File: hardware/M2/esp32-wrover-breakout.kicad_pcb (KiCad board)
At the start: 2 copper layers, 44 x 22 mm, 10 parts, among them IC1 ESP32-WROVER-E_M213EH6464PH3Q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, J1 Edge_Conn_NGFF_E_Key, Q1 MUN5214DW1T1G, U1 XC6220B331MR

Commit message: A couple finishing touches
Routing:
- net GND: track 33.0 -> 32.5 mm
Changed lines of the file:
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@@
     (thickness 1.6)
     (drawings 10)
-    (tracks 320)
+    (tracks 318)
     (zones 0)
     (modules 10)
@@
   (layers
     (0 F.Cu signal)
-    (31 B.Cu signal)
+    (31 B.Cu signal hide)
     (32 B.Adhes user hide)
     (33 F.Adhes user hide)
@@
   (segment (start 68.528 29.399) (end 68.528 28.939) (width 0.25) (layer F.Cu) (net 1))
   (segment (start 68.528 28.939) (end 69.255979 28.211021) (width 0.25) (layer F.Cu) (net 1))
-  (via (at 68.568 31.099) (size 0.508) (drill 0.254) (layers F.Cu B.Cu) (net 1))
-  (segment (start 68.528 29.399) (end 68.528 31.059) (width 0.25) (layer F.Cu) (net 1))
-  (segment (start 68.528 31.059) (end 68.568 31.099) (width 0.25) (layer F.Cu) (net 1))
   (via (at 63.983 35.064) (size 0.508) (drill 0.254) (layers F.Cu B.Cu) (net 1))
   (segment (start 62.863 35.064) (end 63.983 35.064) (width 0.25) (layer F.Cu) (net 1))
@@
   (segment (start 61.028 35.064) (end 61.028 33.959) (width 0.25) (layer F.Cu) (net 1))
   (segment (start 61.028 33.959) (end 61.018 33.949) (width 0.25) (layer F.Cu) (net 1))
-  (via (at 61.018 40.049) (size 0.508) (drill 0.254) (layers F.Cu B.Cu) (net 1))
-  (segment (start 61.028 38.734) (end 61.028 40.039) (width 0.25) (layer F.Cu) (net 1))
-  (segment (start 61.028 40.039) (end 61.018 40.049) (width 0.25) (layer F.Cu) (net 1))
   (via (at 58.068 35.049) (size 0.508) (drill 0.254) (layers F.Cu B.Cu) (net 1))
   (segment (start 59.193 35.064) (end 58.083 35.064) (width 0.25) (layer F.Cu) (net 1))
@@
   (segment (start 68.528 45.009) (end 68.518 44.999) (width 0.25) (layer F.Cu) (net 1))
   (via (at 35.968 47.199) (size 0.508) (drill 0.254) (layers F.Cu B.Cu) (net 1))
+  (via (at 61.028 39.838998) (size 0.508) (drill 0.254) (layers F.Cu B.Cu) (net 1))
+  (segment (start 61.028 38.734) (end 61.028 39.838998) (width 0.25) (layer F.Cu) (net 1))
+  (via (at 68.528 30.809) (size 0.508) (drill 0.254) (layers F.Cu B.Cu) (net 1))
+  (segment (start 68.528 29.399) (end 68.528 30.809) (width 0.25) (layer F.Cu) (net 1))
   (via (at 53.468 32.099) (size 0.508) (drill 0.254) (layers F.Cu B.Cu) (net 3))
   (via (at 54.868 32.099) (size 0.508) (drill 0.254) (layers F.Cu B.Cu) (net 3))

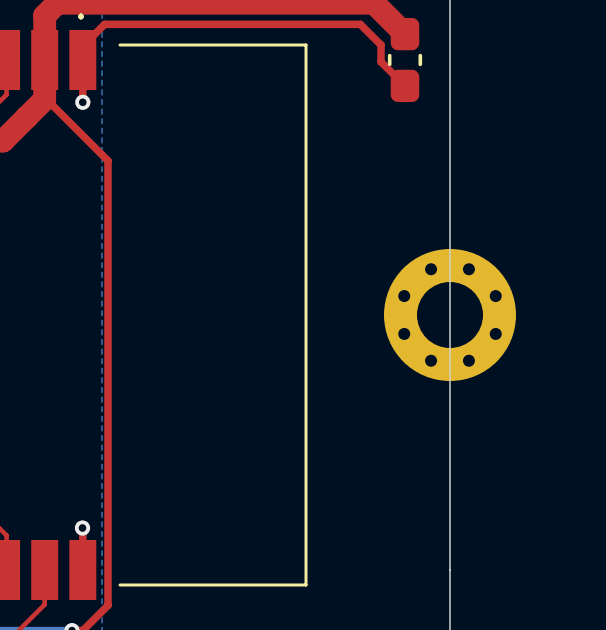
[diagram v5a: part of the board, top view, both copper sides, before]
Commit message: Fix mounting hole size
Allow for the 3mm bushing.
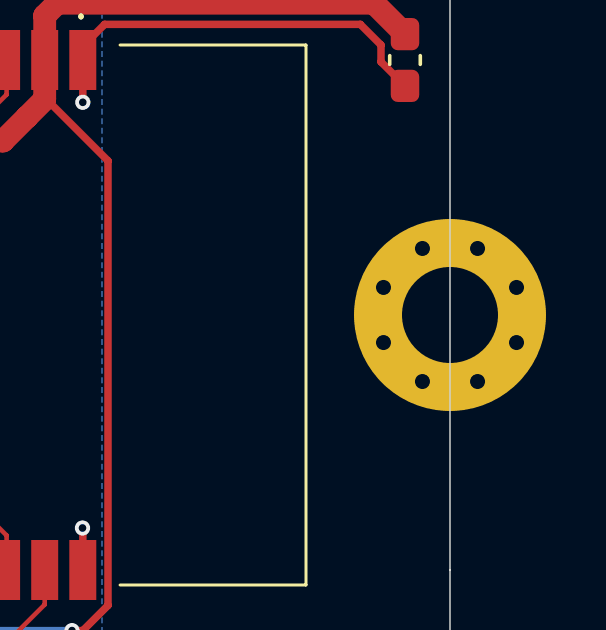
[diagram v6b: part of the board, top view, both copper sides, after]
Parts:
- REF**: value MountingHole_2.2mm_M2_Pad_Via -> MountingHole_3.2mm_M3_Pad_Via; footprint MountingHole:MountingHole_2.2mm_M2_Pad_Via -> MountingHole:MountingHole_3.2mm_M3_Pad_Via
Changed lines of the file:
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@@
     (add_net "Net-(U1-Pad4)")
+  )
+  (module MountingHole:MountingHole_3.2mm_M3_Pad_Via (layer F.Cu)
+    (at 80.768 37.899 22.5)
+    (descr "Mounting Hole 3.2mm, M3")
+    (tags "mounting hole 3.2mm m3")
+    (attr virtual)
+    (fp_text reference REF** (at 0 -3.2 22.5) (layer F.SilkS) hide
+      (effects (font (size 1 1) (thickness 0.15)))
+    )
+    (fp_text value MountingHole_3.2mm_M3_Pad_Via (at 0 3.2 22.5) (layer F.Fab)
+      (effects (font (size 1 1) (thickness 0.15)))
+    )
+    (fp_circle (center 0 0) (end 3.45 0) (layer F.CrtYd) (width 0.05))
+    (fp_circle (center 0 0) (end 3.2 0) (layer Cmts.User) (width 0.15))
+    (fp_text user %R (at 0.3 0 22.5) (layer F.Fab)
+      (effects (font (size 1 1) (thickness 0.15)))
+    )
+    (pad 1 thru_hole circle (at 1.697056 -1.697056 22.5) (size 0.8 0.8) (drill 0.5) (layers *.Cu *.Mask))
+    (pad 1 thru_hole circle (at 0 -2.4 22.5) (size 0.8 0.8) (drill 0.5) (layers *.Cu *.Mask))
+    (pad 1 thru_hole circle (at -1.697056 -1.697056 22.5) (size 0.8 0.8) (drill 0.5) (layers *.Cu *.Mask))
+    (pad 1 thru_hole circle (at -2.4 0 22.5) (size 0.8 0.8) (drill 0.5) (layers *.Cu *.Mask))
+    (pad 1 thru_hole circle (at -1.697056 1.697056 22.5) (size 0.8 0.8) (drill 0.5) (layers *.Cu *.Mask))
+    (pad 1 thru_hole circle (at 0 2.4 22.5) (size 0.8 0.8) (drill 0.5) (layers *.Cu *.Mask))
+    (pad 1 thru_hole circle (at 1.697056 1.697056 22.5) (size 0.8 0.8) (drill 0.5) (layers *.Cu *.Mask))
+    (pad 1 thru_hole circle (at 2.4 0 22.5) (size 0.8 0.8) (drill 0.5) (layers *.Cu *.Mask))
+    (pad 1 thru_hole circle (at 0 0 22.5) (size 6.4 6.4) (drill 3.2) (layers *.Cu *.Mask))
   )
   (module ESP32-WROVER-E:ESP32WROVEREM213EH6464PH3Q0 (layer F.Cu)
@@
       (effects (font (size 1 1) (thickness 0.15)))
     )
-    (fp_arc (start 10.425 -3.5) (end 9.925 -3.5) (angle 90) (layer Edge.Cuts) (width 0.05))
-    (fp_arc (start 2.625 -2.9) (end 2.025 -2.9) (angle 180) (layer Edge.Cuts) (width 0.05))
-    (fp_arc (start -10.425 -3.5) (end -10.425 -4) (angle 90) (layer Edge.Cuts) (width 0.05))
     (fp_line (start -11 -4) (end -10.425 -4) (layer Edge.Cuts) (width 0.05))
     (fp_line (start -9.925 -3.5) (end -9.925 0) (layer Edge.Cuts) (width 0.05))
@@
     (fp_poly (pts (xy 3.225 0) (xy 9.925 0) (xy 9.925 -2) (xy 3.225 -2)) (layer F.Mask) (width 0.1))
     (fp_poly (pts (xy 3.225 0) (xy 9.925 0) (xy 9.925 -2.5) (xy 3.225 -2.5)) (layer B.Mask) (width 0.1))
+    (fp_arc (start 10.425 -3.5) (end 9.925 -3.5) (angle 90) (layer Edge.Cuts) (width 0.05))
+    (fp_arc (start 2.625 -2.9) (end 2.025 -2.9) (angle 180) (layer Edge.Cuts) (width 0.05))
+    (fp_arc (start -10.425 -3.5) (end -10.425 -4) (angle 90) (layer Edge.Cuts) (width 0.05))
     (pad 75 smd rect (at -9.25 -1.275 270) (size 0.35 1.45) (layers F.Cu)
       (net 1 GND))
@@
     (pad 1 smd rect (at 9.25 -1.275 270) (size 0.35 1.45) (layers F.Cu)
       (net 1 GND))
-  )
-  (module MountingHole:MountingHole_2.2mm_M2_Pad_Via (layer F.Cu)
-    (at 80.768 37.899 22.5)
-    (descr "Mounting Hole 2.2mm, M2")
-    (tags "mounting hole 2.2mm m2")
-    (attr virtual)
-    (fp_text reference REF** (at 0 -3.2 22.5) (layer F.SilkS) hide
-      (effects (font (size 1 1) (thickness 0.15)))
-    )
-    (fp_text value MountingHole_2.2mm_M2_Pad_Via (at 0 3.2 22.5) (layer F.Fab)
-      (effects (font (size 1 1) (thickness 0.15)))
-    )
-    (fp_text user %R (at 0.3 0 22.5) (layer F.Fab)
-      (effects (font (size 1 1) (thickness 0.15)))
-    )
-    (fp_circle (center 0 0) (end 2.2 0) (layer Cmts.User) (width 0.15))
-    (fp_circle (center 0 0) (end 2.45 0) (layer F.CrtYd) (width 0.05))
-    (pad 1 thru_hole circle (at 1.166726 -1.166726 22.5) (size 0.7 0.7) (drill 0.4) (layers *.Cu *.Mask))
-    (pad 1 thru_hole circle (at 0 -1.65 22.5) (size 0.7 0.7) (drill 0.4) (layers *.Cu *.Mask))
-    (pad 1 thru_hole circle (at -1.166726 -1.166726 22.5) (size 0.7 0.7) (drill 0.4) (layers *.Cu *.Mask))
-    (pad 1 thru_hole circle (at -1.65 0 22.5) (size 0.7 0.7) (drill 0.4) (layers *.Cu *.Mask))
-    (pad 1 thru_hole circle (at -1.166726 1.166726 22.5) (size 0.7 0.7) (drill 0.4) (layers *.Cu *.Mask))
-    (pad 1 thru_hole circle (at 0 1.65 22.5) (size 0.7 0.7) (drill 0.4) (layers *.Cu *.Mask))
-    (pad 1 thru_hole circle (at 1.166726 1.166726 22.5) (size 0.7 0.7) (drill 0.4) (layers *.Cu *.Mask))
-    (pad 1 thru_hole circle (at 1.65 0 22.5) (size 0.7 0.7) (drill 0.4) (layers *.Cu *.Mask))
-    (pad 1 thru_hole circle (at 0 0 22.5) (size 4.4 4.4) (drill 2.2) (layers *.Cu *.Mask))
   )
   (module MUN5214DW1T1G:On_Semiconductor-MUN5214DW1T1G-Manufacturer_Recommended (layer F.Cu)
@@
       (effects (font (size 1 1) (thickness 0.15)))
     )
-    (fp_text user %R (at 0 0 90) (layer F.Fab)
-      (effects (font (size 0.4 0.4) (thickness 0.06)))
-    )
     (fp_line (start -0.8 0.4) (end -0.8 -0.4) (layer F.Fab) (width 0.1))
     (fp_line (start -0.8 -0.4) (end 0.8 -0.4) (layer F.Fab) (width 0.1))
@@
     (fp_line (start 1.65 -0.73) (end 1.65 0.73) (layer F.CrtYd) (width 0.05))
     (fp_line (start 1.65 0.73) (end -1.65 0.73) (layer F.CrtYd) (width 0.05))
+    (fp_text user %R (at 0 0 90) (layer F.Fab)
+      (effects (font (size 0.4 0.4) (thickness 0.06)))
+    )
     (pad 2 smd roundrect (at 0.8625 0 270) (size 1.075 0.95) (layers F.Cu F.Paste F.Mask) (roundrect_rratio 0.25)
       (net 1 GND))
@@
     (fp_text value 10k (at 0 1.43) (layer F.Fab)
       (effects (font (size 1 1) (thickness 0.15)))
-    )
-    (fp_text user %R (at 0 0) (layer F.Fab)
-      (effects (font (size 0.4 0.4) (thickness 0.06)))
     )
     (fp_line (start -0.8 0.4125) (end -0.8 -0.4125) (layer F.Fab) (width 0.1))
@@
     (fp_line (start 1.65 -0.73) (end 1.65 0.73) (layer F.CrtYd) (width 0.05))
     (fp_line (start 1.65 0.73) (end -1.65 0.73) (layer F.CrtYd) (width 0.05))
+    (fp_text user %R (at 0 0) (layer F.Fab)
+      (effects (font (size 0.4 0.4) (thickness 0.06)))
+    )
     (pad 1 smd roundrect (at -0.9125 0) (size 0.975 0.95) (layers F.Cu F.Paste F.Mask) (roundrect_rratio 0.25)
       (net 3 +3V3))
@@
       (effects (font (size 1 1) (thickness 0.15)))
     )
-    (fp_text user %R (at 0 0) (layer F.Fab)
-      (effects (font (size 0.4 0.4) (thickness 0.06)))
-    )
     (fp_line (start -0.8 0.4) (end -0.8 -0.4) (layer F.Fab) (width 0.1))
     (fp_line (start -0.8 -0.4) (end 0.8 -0.4) (layer F.Fab) (width 0.1))
@@
     (fp_line (start 1.65 -0.73) (end 1.65 0.73) (layer F.CrtYd) (width 0.05))
     (fp_line (start 1.65 0.73) (end -1.65 0.73) (layer F.CrtYd) (width 0.05))
+    (fp_text user %R (at 0 0) (layer F.Fab)
+      (effects (font (size 0.4 0.4) (thickness 0.06)))
+    )
     (pad 1 smd roundrect (at -0.8625 0 180) (size 1.075 0.95) (layers F.Cu F.Paste F.Mask) (roundrect_rratio 0.25)
       (net 4 /RESET))
@@
   )
   (gr_line (start 40.168 68.899) (end 61.368 68.899) (layer Dwgs.User) (width 0.05))
-  (gr_text "François Gervais\n12 jan 2021\nrev 2.0" (at 75.268 47.899 270) (layer B.SilkS)
+  (gr_text "François Gervais\n12 jan 2021\nrev 2.0" (at 74.268 47.899 270) (layer B.SilkS)
     (effects (font (size 1 1) (thickness 0.15)) (justify left mirror))
   )
@@
   (via (at 68.528 30.809) (size 0.508) (drill 0.254) (layers F.Cu B.Cu) (net 1))
   (segment (start 68.528 29.399) (end 68.528 30.809) (width 0.25) (layer F.Cu) (net 1))
-  (via (at 53.468 32.099) (size 0.508) (drill 0.254) (layers F.Cu B.Cu) (net 3))
-  (via (at 54.868 32.099) (size 0.508) (drill 0.254) (layers F.Cu B.Cu) (net 3))
-  (via (at 54.168 32.099) (size 0.508) (drill 0.254) (layers F.Cu B.Cu) (net 3))
-  (via (at 55.568 32.099) (size 0.508) (drill 0.254) (layers F.Cu B.Cu) (net 3))
-  (segment (start 61.268 32.099) (end 61.268 32.099) (width 0.762) (layer B.Cu) (net 3))
-  (via (at 61.268 32.099) (size 0.508) (drill 0.254) (layers F.Cu B.Cu) (net 3))
   (segment (start 35.318 29.399) (end 34.293 29.399) (width 0.25) (layer B.Cu) (net 2))
   (segment (start 34.293 28.899) (end 35.318 28.899) (width 0.25) (layer B.Cu) (net 2))
@@
   (segment (start 38.318 32.199) (end 38.318 32.349) (width 0.762) (layer B.Cu) (net 2))
   (via (at 38.318 32.199) (size 0.508) (drill 0.254) (layers F.Cu B.Cu) (net 2))
+  (segment (start 35.568 29.149) (end 35.318 29.399) (width 0.25) (layer B.Cu) (net 2))
+  (segment (start 35.318 28.899) (end 35.568 29.149) (width 0.25) (layer B.Cu) (net 2))
+  (segment (start 35.568 29.149) (end 37.318 29.149) (width 0.762) (layer B.Cu) (net 2))
+  (via (at 53.468 32.099) (size 0.508) (drill 0.254) (layers F.Cu B.Cu) (net 3))
+  (via (at 54.868 32.099) (size 0.508) (drill 0.254) (layers F.Cu B.Cu) (net 3))
+  (via (at 54.168 32.099) (size 0.508) (drill 0.254) (layers F.Cu B.Cu) (net 3))
+  (via (at 55.568 32.099) (size 0.508) (drill 0.254) (layers F.Cu B.Cu) (net 3))
+  (segment (start 61.268 32.099) (end 61.268 32.099) (width 0.762) (layer B.Cu) (net 3))
+  (via (at 61.268 32.099) (size 0.508) (drill 0.254) (layers F.Cu B.Cu) (net 3))
   (segment (start 67.258 29.399) (end 67.258 30.709) (width 0.762) (layer F.Cu) (net 3))
   (segment (start 67.258 30.709) (end 66.668 31.299) (width 0.762) (layer F.Cu) (net 3))
@@
   (segment (start 57.098 28.2466) (end 56.2504 27.399) (width 0.1524) (layer F.Cu) (net 39))
   (segment (start 56.2504 27.399) (end 38.968 27.399) (width 0.1524) (layer F.Cu) (net 39))
-  (segment (start 35.568 29.149) (end 35.318 29.399) (width 0.25) (layer B.Cu) (net 2))
-  (segment (start 35.318 28.899) (end 35.568 29.149) (width 0.25) (layer B.Cu) (net 2))
-  (segment (start 35.568 29.149) (end 37.318 29.149) (width 0.762) (layer B.Cu) (net 2))
   (zone (net 2) (net_name +5V) (layer F.Cu) (hatch edge 0.508)
     (connect_pads (clearance 0.1524))

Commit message: Add version of previous commit
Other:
- board text added: "François Gervais 10 fev 2021 v2.0-8-g032313b"
- board text removed: "François Gervais 12 jan 2021 rev 2.0"

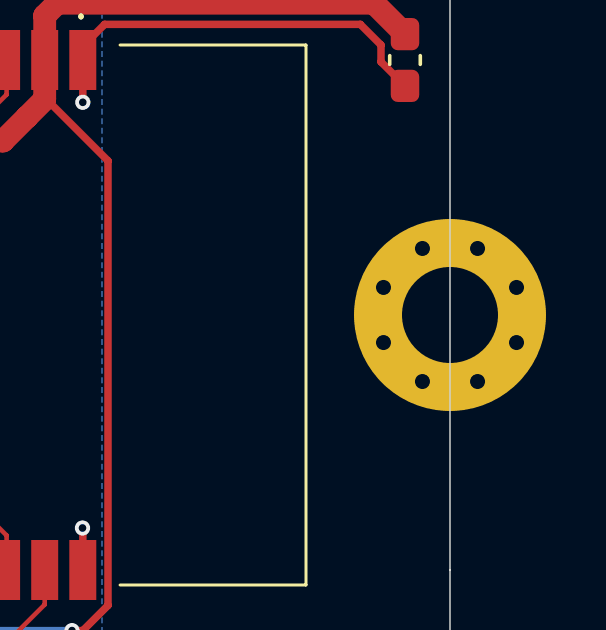
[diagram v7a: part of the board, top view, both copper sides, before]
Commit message: Change the mounting hole size
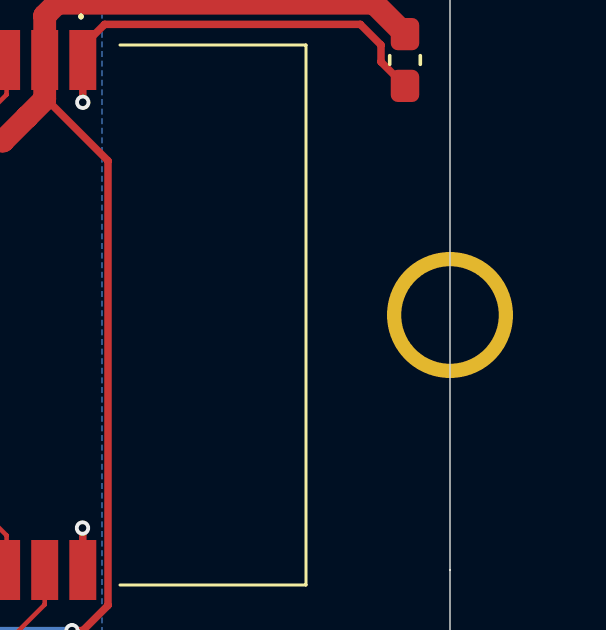
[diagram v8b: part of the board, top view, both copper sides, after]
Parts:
- REF**: value MountingHole_3.2mm_M3_Pad_Via -> MountingHole_3.2mm_M3_Pad; footprint MountingHole:MountingHole_3.2mm_M3_Pad_Via -> MountingHole:MountingHole_3.2mm_M3_Pad
